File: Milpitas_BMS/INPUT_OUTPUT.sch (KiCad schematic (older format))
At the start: 46 parts, among them J400 CHG INPUT, J401 POWER_OUTPUT, J402 BATT_PWR_INPUT, Q400 RU1J002YNTCL, Q401 RU1J002YNTCL, Q402 RU1J002YNTCL, U400 ACS711, U401 BTS6163DAUMA1, U402 ACS711, U403 BTS6163DAUMA1, U404 BTS6163DAUMA1, U405 ACS711

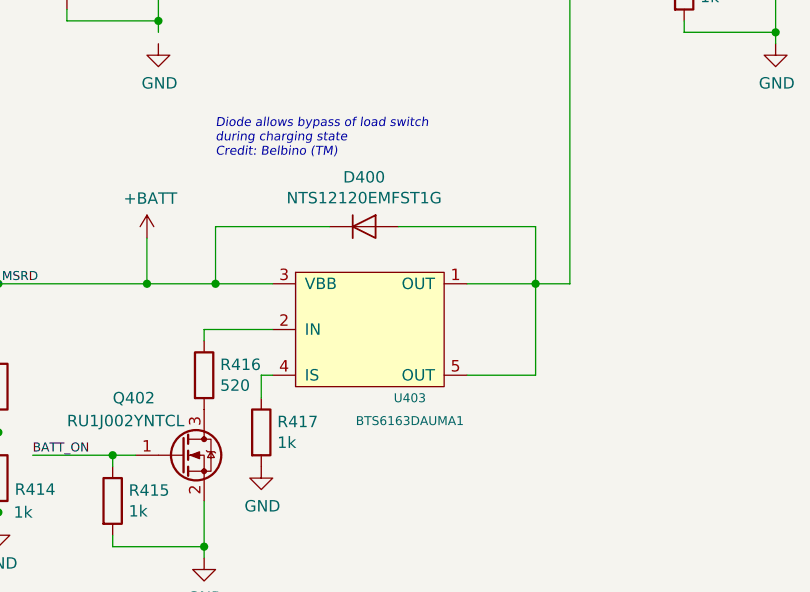
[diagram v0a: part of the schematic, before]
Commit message: updated some parts to inclued footprints + digikey P/N
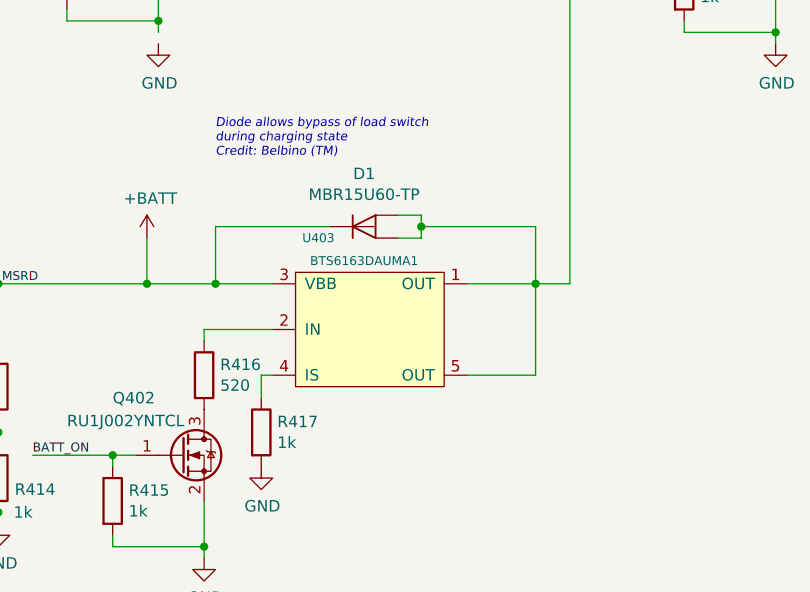
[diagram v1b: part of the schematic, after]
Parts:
- removed D400: NTS12120EMFST1G, symbol Device:D
- added D1: MBR15U60-TP, Package_TO_SOT_SMD:TO-277A, symbol Milipitas:MBR15U60-TP
- C400, C401, C402, C403, C404, C405, C406, C407, C408: footprint (none) -> Capacitor_SMD:C_0603_1608Metric
- F400, F401, F402: footprint (none) -> Fuse:Fuse_1206_3216Metric; Digikey (none) -> 486-1686-1-ND
- R400, R401, R402, R403, R404, R405, R406, R407, R408, R409, R410, R411, R412, R414, R415, R416, R417, R418: footprint (none) -> Resistor_SMD:R_0603_1608Metric
- U401, U404: footprint (none) -> Package_TO_SOT_SMD:TO-252-5_TabPin3; Digikey (none) -> BTS6163DAUMA1CT-ND
- U403: footprint (none) -> Package_TO_SOT_SMD:TO-252-5_TabPin3
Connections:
- net +BATT: now also D1.3 (K)
- net MIXED_PWR_PLANE: now also D1.1 (A), D1.2 (A)

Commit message: lots of little fixes
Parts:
- J400, J401, J402: footprint (none) -> Milpitas_BMS:XT30-RIGHT-ANGLE
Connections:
- net GND: now also Q400.2 (S), R403.2
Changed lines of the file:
@@
 F 0 "J402" H 592 3875 50  0000 C CNN
 F 1 "BATT_PWR_INPUT" H 592 3966 50  0000 C CNN
-F 2 "" H 700 4200 50  0001 C CNN
-F 3 "~" H 700 4200 50  0001 C CNN
+F 2 "Milpitas_BMS:XT30-RIGHT-ANGLE" H 700 4200 50  0001 C CNN
+F 3 "https://www.aliexpress.com/item/32689137918.html" H 700 4200 50  0001 C CNN
 	1    700  4200
 	-1   0    0    1
@@
 F 0 "J400" H 492 1625 50  0000 C CNN
 F 1 "CHG INPUT" H 492 1716 50  0000 C CNN
-F 2 "" H 600 1950 50  0001 C CNN
-F 3 "~" H 600 1950 50  0001 C CNN
+F 2 "Milpitas_BMS:XT30-RIGHT-ANGLE" H 600 1950 50  0001 C CNN
+F 3 "https://www.aliexpress.com/item/32689137918.html" H 600 1950 50  0001 C CNN
 	1    600  1950
 	-1   0    0    1
@@
 Wire Wire Line
 	4350 4100 4600 4100
-Text Label 7850 4350 0    39   ~ 0
-BATT_ON
-Text Label 7850 3550 0    39   ~ 0
-CHG_ON
-Text Label 7850 3950 0    39   ~ 0
-DIS_ON
-Wire Wire Line
-	8300 4050 7850 4050
-Wire Wire Line
-	8300 3950 7850 3950
-Wire Wire Line
-	8300 3850 7850 3850
-Wire Wire Line
-	8300 3750 7850 3750
-Wire Wire Line
-	8300 3550 7850 3550
-Entry Wire Line
-	8300 3550 8400 3650
-Entry Wire Line
-	8300 3650 8400 3750
-Entry Wire Line
-	8300 3750 8400 3850
-Entry Wire Line
-	8300 3850 8400 3950
-Entry Wire Line
-	8300 3950 8400 4050
-Entry Wire Line
-	8300 4050 8400 4150
-Text HLabel 8600 4800 2    39   Input ~ 0
-STM_32_IO_CTL
 $Comp
 L power:+BATT #PWR0142
@@
 	5900 4100 5900 1850
 Wire Wire Line
-	8300 3650 7850 3650
-Wire Wire Line
 	1850 2000 1650 2000
 Wire Wire Line
@@
 L power:GND #PWR0151
 U 1 1 617E3F94
-P 4100 3050
-F 0 "#PWR0151" H 4100 2800 50  0001 C CNN
-F 1 "GND" H 4105 2877 50  0000 C CNN
-F 2 "" H 4100 3050 50  0001 C CNN
-F 3 "" H 4100 3050 50  0001 C CNN
-	1    4100 3050
+P 4100 3000
+F 0 "#PWR0151" H 4100 2750 50  0001 C CNN
+F 1 "GND" H 4105 2827 50  0000 C CNN
+F 2 "" H 4100 3000 50  0001 C CNN
+F 3 "" H 4100 3000 50  0001 C CNN
+	1    4100 3000
 	1    0    0    -1
 $EndComp
@@
 F 0 "J401" H 10892 1625 50  0000 C CNN
 F 1 "POWER_OUTPUT" H 10892 1716 50  0000 C CNN
-F 2 "" H 11000 1950 50  0001 C CNN
-F 3 "~" H 11000 1950 50  0001 C CNN
+F 2 "Milpitas_BMS:XT30-RIGHT-ANGLE" H 11000 1950 50  0001 C CNN
+F 3 "https://www.aliexpress.com/item/32689137918.html" H 11000 1950 50  0001 C CNN
 	1    11000 1950
 	1    0    0    1
@@
 	9700 1850 10200 1850
 Connection ~ 9800 2500
-Text Label 7850 3850 0    39   ~ 0
-CHG_FAULT
-Text Label 7850 3750 0    39   ~ 0
-I_CHG
-Text Label 7850 3650 0    39   ~ 0
-V_CHG
-Wire Wire Line
-	7850 4150 8300 4150
-Wire Wire Line
-	7850 4250 8300 4250
-Wire Wire Line
-	7850 4350 8300 4350
-Wire Wire Line
-	7850 4450 8300 4450
-Wire Wire Line
-	7850 4550 8300 4550
-Wire Wire Line
-	7850 4650 8300 4650
-Wire Bus Line
-	8400 4800 8600 4800
-Text Label 7850 4150 0    39   ~ 0
-I_DIS
-Text Label 7850 4250 0    39   ~ 0
-DIS_FAULT
-Text Label 7850 4050 0    39   ~ 0
-V_DIS
-Text Label 7850 4450 0    39   ~ 0
-V_BATT
-Text Label 7850 4550 0    39   ~ 0
-I_BATT
-Text Label 7850 4650 0    39   ~ 0
-BATT_FAULT
-Entry Wire Line
-	8300 4150 8400 4250
-Entry Wire Line
-	8300 4250 8400 4350
-Entry Wire Line
-	8300 4350 8400 4450
-Entry Wire Line
-	8300 4450 8400 4550
-Entry Wire Line
-	8300 4550 8400 4650
-Entry Wire Line
-	8300 4650 8400 4750
 $Sheet
 S 1050 6000 2250 1100
@@
 F0 "Cell Tap Pinout" 39
 F1 "Cell_Tap_Pinout.sch" 39
-F2 "BUS_SOUTH_CELL_CONN" I R 3300 6900 39
-F3 "BUS_NORTH_CELL_CONN" I R 3300 7000 39
 $EndSheet
 Text Notes 1450 6700 0    157  ~ 31
 CELL TAP \nCONNECTORS
-Text HLabel 3650 6900 2    39   Input ~ 0
-BUS_SOUTH_CELL_CONN
-Text HLabel 3650 7000 2    39   Input ~ 0
-BUS_NORTH_CELL_CONN
-Wire Bus Line
-	3300 6900 3650 6900
-Wire Bus Line
-	3300 7000 3650 7000
 Text Notes 650  1550 0    39   ~ 0
 XT30
@@
 Wire Wire Line
 	5250 3800 5150 3800
-Wire Bus Line
-	8400 3650 8400 4800
 Connection ~ 5250 3850
 $Comp

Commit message: For review call
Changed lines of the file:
@@
 Text Notes 4350 3550 0    39   Italic 0
 Diode allows bypass of load switch\nduring charging state\nCredit: Belbino (TM)\n
-Text Notes 9200 4450 0    39   ~ 0
+Text Notes 8000 4550 0    39   ~ 0
 FOUR BMS States:\nCharging, Discharging, Standby, Fault\nThree load switches:\nCHG | DIS | BATT\nCharge state: 1 | x | 0\nDischarge State: x | 1 | 1\nFault : 0 | 0 | 0
 $Comp
@@
 	0    -1   -1   0
 $EndComp
+Wire Wire Line
+	7250 4550 6900 4550
+Wire Wire Line
+	7250 4950 6900 4950
+Wire Wire Line
+	7250 4150 6900 4150
+Text Label 6900 4150 0    39   ~ 0
+DIS_FAULT
+Text Label 6900 4550 0    39   ~ 0
+BATT_FAULT
+Wire Wire Line
+	7250 3850 6900 3850
+Wire Wire Line
+	7250 4250 6900 4250
+Text Label 6900 3850 0    39   ~ 0
+DIS_ON
+Text Label 6900 4950 0    39   ~ 0
+CHG_FAULT
+Text Label 6900 4350 0    39   ~ 0
+I_BATT
+Text Label 6900 4450 0    39   ~ 0
+V_BATT
+Text Label 6900 4750 0    39   ~ 0
+I_CHG
+Text Label 6900 4050 0    39   ~ 0
+V_DIS
+Wire Wire Line
+	7250 4350 6900 4350
+Wire Wire Line
+	7250 4450 6900 4450
+Wire Wire Line
+	7250 4750 6900 4750
+Wire Wire Line
+	7250 4050 6900 4050
+Text Label 6900 3950 0    39   ~ 0
+I_DIS
+Wire Wire Line
+	7250 3950 6900 3950
+Wire Wire Line
+	7250 4850 6900 4850
+Text Label 6900 4850 0    39   ~ 0
+V_CHG
+Text Label 6900 4250 0    39   ~ 0
+BATT_ON
+Text Label 6900 4650 0    39   ~ 0
+CHG_ON
+Wire Wire Line
+	7250 4650 6900 4650
+Text GLabel 7250 3850 2    39   Input ~ 0
+DIS_ON
+Text GLabel 7250 3950 2    39   Input ~ 0
+I_DIS
+Text GLabel 7250 4050 2    39   Input ~ 0
+V_DIS
+Text GLabel 7250 4150 2    39   Input ~ 0
+DIS_FAULT
+Text GLabel 7250 4250 2    39   Input ~ 0
+BATT_ON
+Text GLabel 7250 4350 2    39   Input ~ 0
+I_BATT
+Text GLabel 7250 4450 2    39   Input ~ 0
+V_BATT
+Text GLabel 7250 4550 2    39   Input ~ 0
+BATT_FAULT
+Text GLabel 7250 4650 2    39   Input ~ 0
+CHG_ON
+Text GLabel 7250 4750 2    39   Input ~ 0
+I_CHG
+Text GLabel 7250 4850 2    39   Input ~ 0
+V_CHG
+Text GLabel 7250 4950 2    39   Input ~ 0
+CHG_FAULT
 $EndSCHEMATC

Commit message: (maybe) final placement V1,0
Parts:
- TP401, TP402: footprint (none) -> TestPoint:TestPoint_Pad_D1.0mm
- U400, U402, U405: footprint Sensor_Current:Allegro_QFN-12-10-1EP_3x3mm_P0.5mm -> Milpitas_BMS:Allegro_QFN-12-10-1EP_3x3mm_P0.5mm
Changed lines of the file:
@@
 F 0 "U400" H 2100 2000 39  0000 L CNN
 F 1 "ACS711" H 2050 1950 39  0000 L CNN
-F 2 "Sensor_Current:Allegro_QFN-12-10-1EP_3x3mm_P0.5mm" H 2350 1850 39  0001 C CNN
+F 2 "Milpitas_BMS:Allegro_QFN-12-10-1EP_3x3mm_P0.5mm" H 2350 1850 39  0001 C CNN
 F 3 "" H 2350 1850 39  0001 C CNN
 F 4 "620-1483-1-ND" H 2350 1850 50  0001 C CNN "Digikey"
@@
 F 0 "U402" H 2150 4300 39  0000 L CNN
 F 1 "ACS711" H 2100 4200 39  0000 L CNN
-F 2 "Sensor_Current:Allegro_QFN-12-10-1EP_3x3mm_P0.5mm" H 2400 4100 39  0001 C CNN
+F 2 "Milpitas_BMS:Allegro_QFN-12-10-1EP_3x3mm_P0.5mm" H 2400 4100 39  0001 C CNN
 F 3 "" H 2400 4100 39  0001 C CNN
 F 4 "620-1483-1-ND" H 2400 4100 50  0001 C CNN "Digikey"
@@
 F 0 "U405" H 9700 1750 39  0000 L CNN
 F 1 "ACS711" H 9650 1650 39  0000 L CNN
-F 2 "Sensor_Current:Allegro_QFN-12-10-1EP_3x3mm_P0.5mm" H 9150 1850 39  0001 C CNN
+F 2 "Milpitas_BMS:Allegro_QFN-12-10-1EP_3x3mm_P0.5mm" H 9150 1850 39  0001 C CNN
 F 3 "" H 9150 1850 39  0001 C CNN
 F 4 "620-1483-1-ND" H 9150 1850 50  0001 C CNN "Digikey"
@@
 Wire Wire Line
 	1350 1850 1850 1850
-$Comp
-L Connector:TestPoint TP402
-U 1 1 6263465D
-P 10200 1250
-F 0 "TP402" H 10258 1368 50  0000 L CNN
-F 1 "DISCHARGE" H 10258 1277 50  0000 L CNN
-F 2 "" H 10400 1250 50  0001 C CNN
-F 3 "~" H 10400 1250 50  0001 C CNN
-	1    10200 1250
-	1    0    0    -1
-$EndComp
 Wire Wire Line
 	10200 1850 10200 1250
-$Comp
-L Connector:TestPoint TP401
-U 1 1 626433EB
-P 5900 1300
-F 0 "TP401" H 5958 1418 50  0000 L CNN
-F 1 "POWER_MIX" H 5958 1327 50  0000 L CNN
-F 2 "" H 6100 1300 50  0001 C CNN
-F 3 "~" H 6100 1300 50  0001 C CNN
-	1    5900 1300
-	1    0    0    -1
-$EndComp
 Wire Wire Line
 	5900 1850 5900 1300
@@
 Text GLabel 7250 4950 2    39   Input ~ 0
 CHG_FAULT
+$Comp
+L Connector:TestPoint TP?
+U 1 1 5FCA12D8
+P 5900 1300
+AR Path="/5FD707DF/5FCA12D8" Ref="TP?"  Part="1"
+AR Path="/5FD4A06E/5FCA12D8" Ref="TP401"  Part="1"
+F 0 "TP401" H 5958 1418 50  0000 L CNN
+F 1 "POWER_MIX" H 5958 1327 50  0000 L CNN
+F 2 "TestPoint:TestPoint_Pad_D1.0mm" H 6100 1300 50  0001 C CNN
+F 3 "" H 6100 1300 50  0001 C CNN
+F 4 "" H 5900 1300 50  0001 C CNN "Digikey"
+	1    5900 1300
+	1    0    0    -1
+$EndComp
+$Comp
+L Connector:TestPoint TP?
+U 1 1 5FCA7AF1
+P 10200 1250
+AR Path="/5FD707DF/5FCA7AF1" Ref="TP?"  Part="1"
+AR Path="/5FD4A06E/5FCA7AF1" Ref="TP402"  Part="1"
+F 0 "TP402" H 10258 1368 50  0000 L CNN
+F 1 "DISCHARGE" H 10258 1277 50  0000 L CNN
+F 2 "TestPoint:TestPoint_Pad_D1.0mm" H 10400 1250 50  0001 C CNN
+F 3 "" H 10400 1250 50  0001 C CNN
+F 4 "" H 10200 1250 50  0001 C CNN "Digikey"
+	1    10200 1250
+	1    0    0    -1
+$EndComp
 $EndSCHEMATC

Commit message: First pass routing
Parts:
- TP400: footprint (none) -> TestPoint:TestPoint_Pad_D1.0mm
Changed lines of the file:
@@
 F 0 "TP400" H 1408 1368 50  0000 L CNN
 F 1 "CHARGER" H 1408 1277 50  0000 L CNN
-F 2 "" H 1550 1250 50  0001 C CNN
+F 2 "TestPoint:TestPoint_Pad_D1.0mm" H 1550 1250 50  0001 C CNN
 F 3 "~" H 1550 1250 50  0001 C CNN
 	1    1350 1250
